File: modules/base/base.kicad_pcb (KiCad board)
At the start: 2 copper layers, 200.7 x 160 mm, 26 parts

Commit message: Add the version text
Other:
- board text added: "BASE 0.1.0"
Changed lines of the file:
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@@
+		)
+	)
+	(gr_text "BASE\n0.1.0"
+		(at 233.68 175.26 0)
+		(layer "F.SilkS")
+		(effects
+			(font
+				(size 2 2)
+				(thickness 0.4)
+				(bold yes)
+			)
+			(justify right bottom)
 		)
 	)

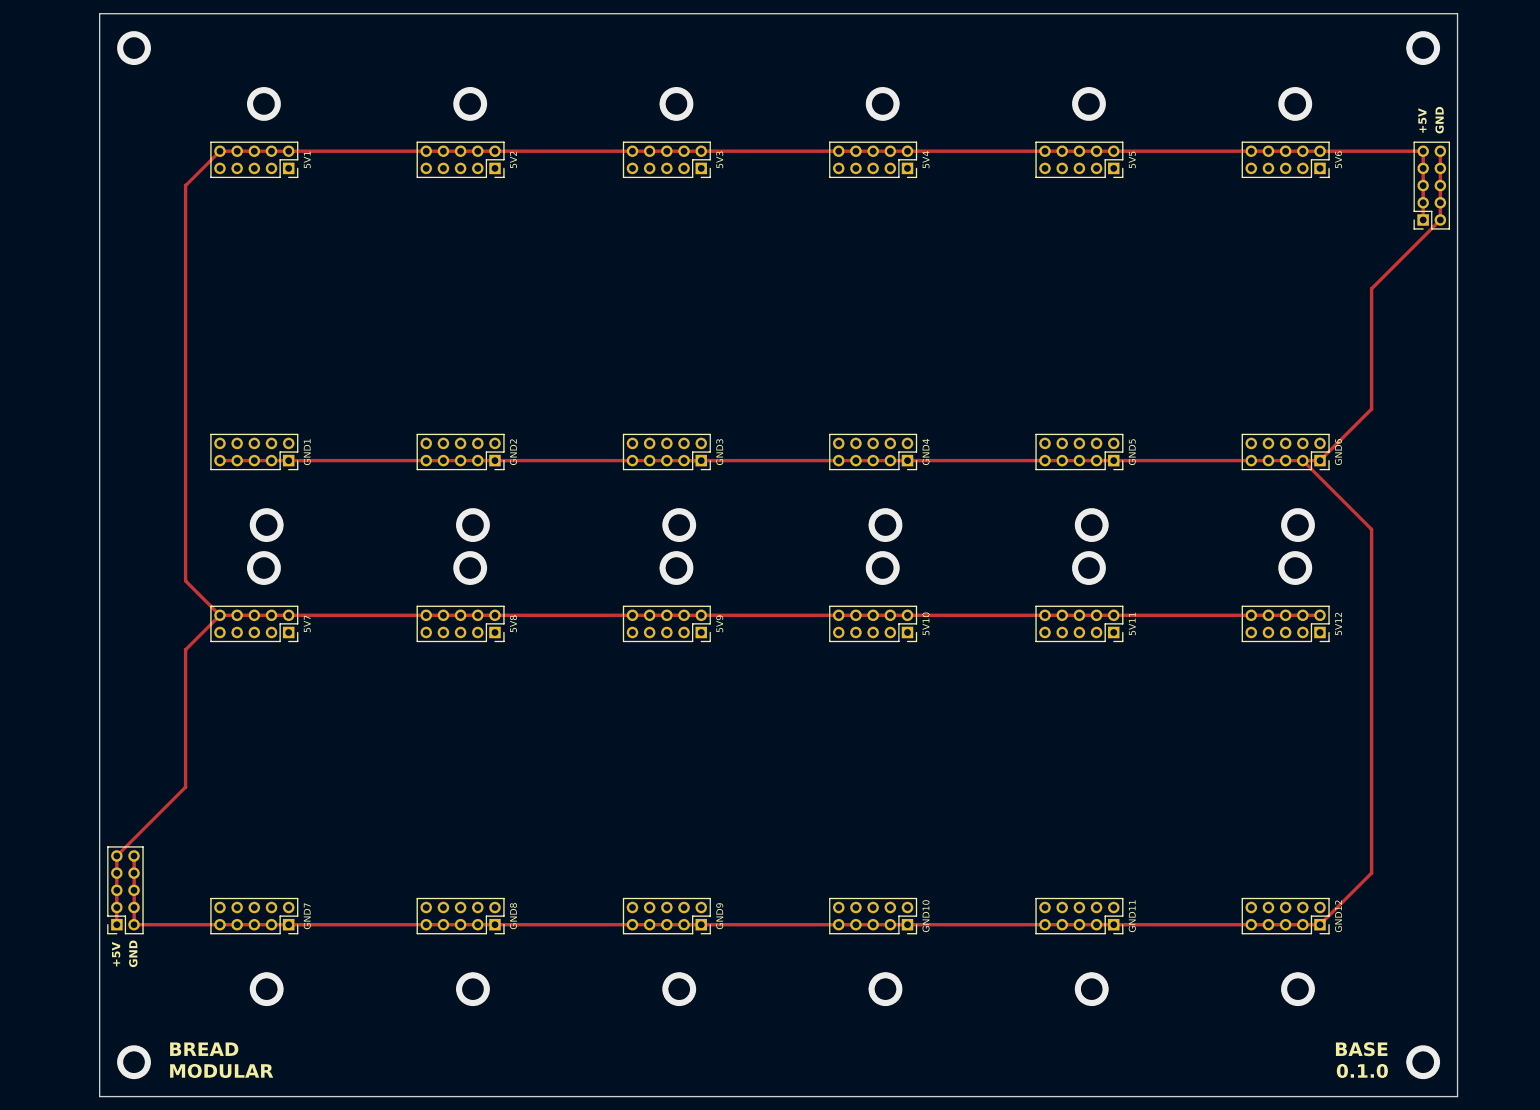
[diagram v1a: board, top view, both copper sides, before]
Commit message: Add power/gnd jacks
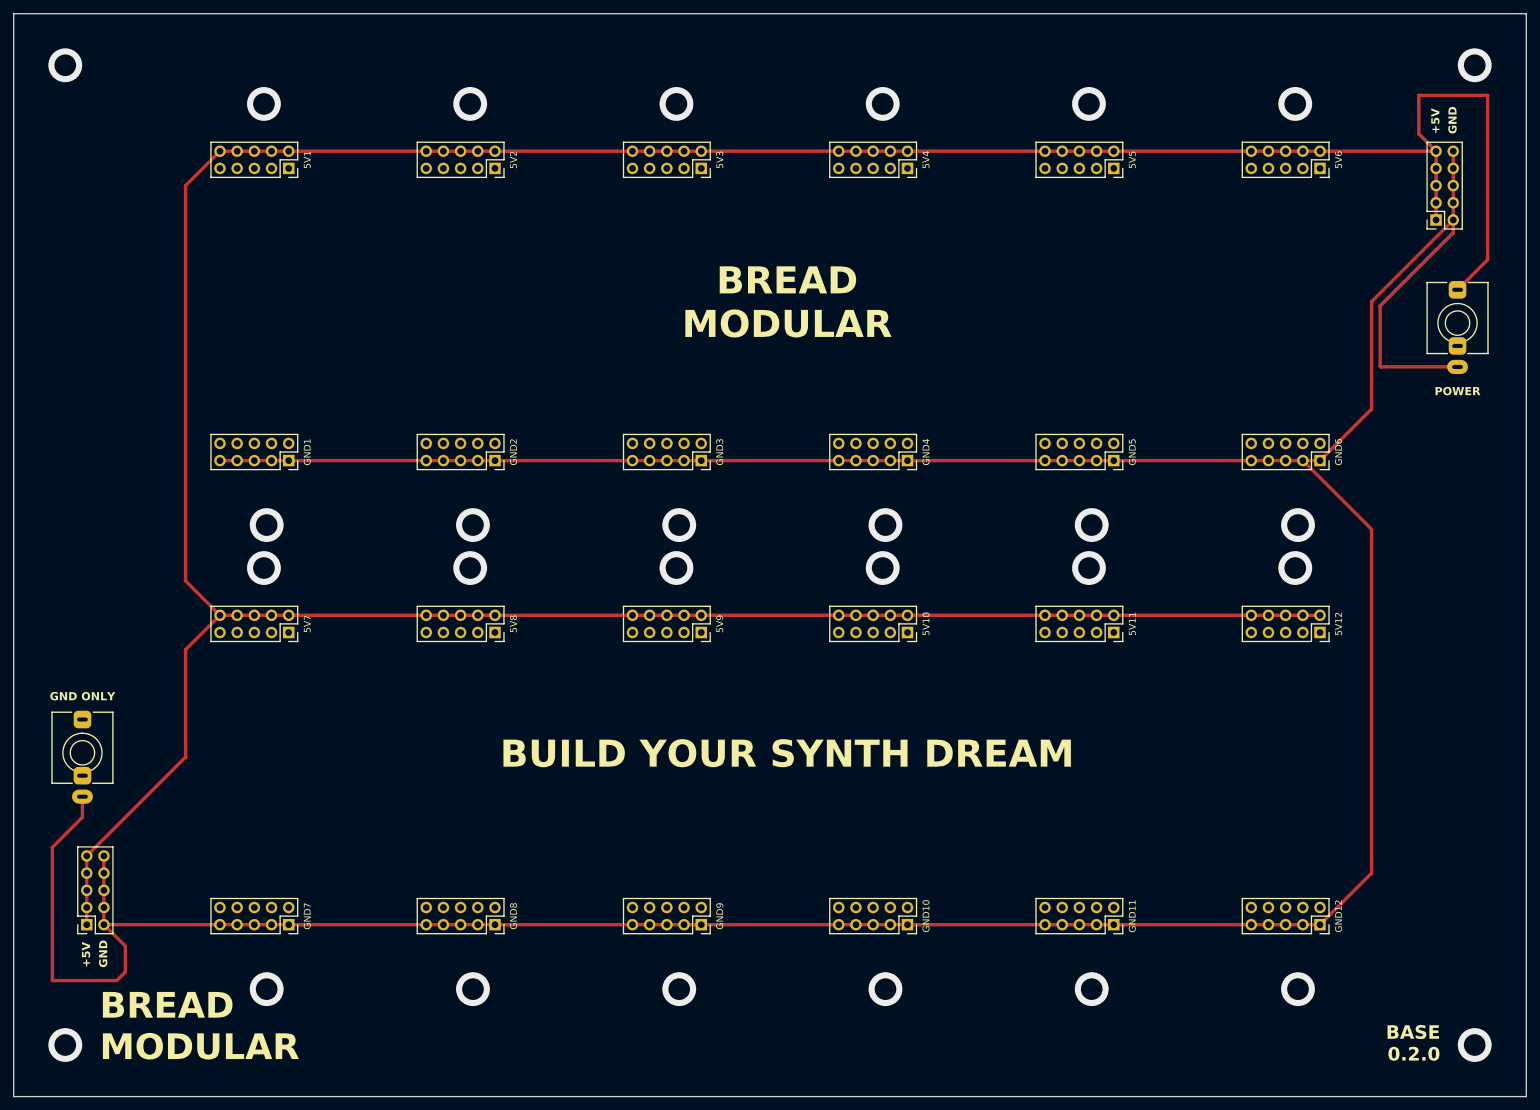
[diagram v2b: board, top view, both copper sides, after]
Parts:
- added J1: Power, BreadModular_AudioJacks:Jack_3.5mm_QingPu_WQP-PJ366ST_Vertical, F.Cu at (243.8, 63.5)
- added J2: Ground, BreadModular_AudioJacks:Jack_3.5mm_QingPu_WQP-PJ366ST_Vertical, F.Cu at (40.6, 127.0)
- moved 5V14 4.45 mm to (41.3, 152.4)
- moved 5V13 1.91 mm to (240.7, 48.3)
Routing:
- net GND: track 477.0 -> 568.4 mm
- net +5V: track 475.3 -> 529.1 mm
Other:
- board size 200.7 x 160 mm -> 223.5 x 160 mm
- board text added: "BASE 0.2.0"
- board text added: "BUILD YOUR SYNTH DREAM"
- board text added: "GND ONLY"
- board text added: "POWER"
- board text removed: "BASE 0.1.0"

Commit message: Add 2 jack sockets for cascading support.
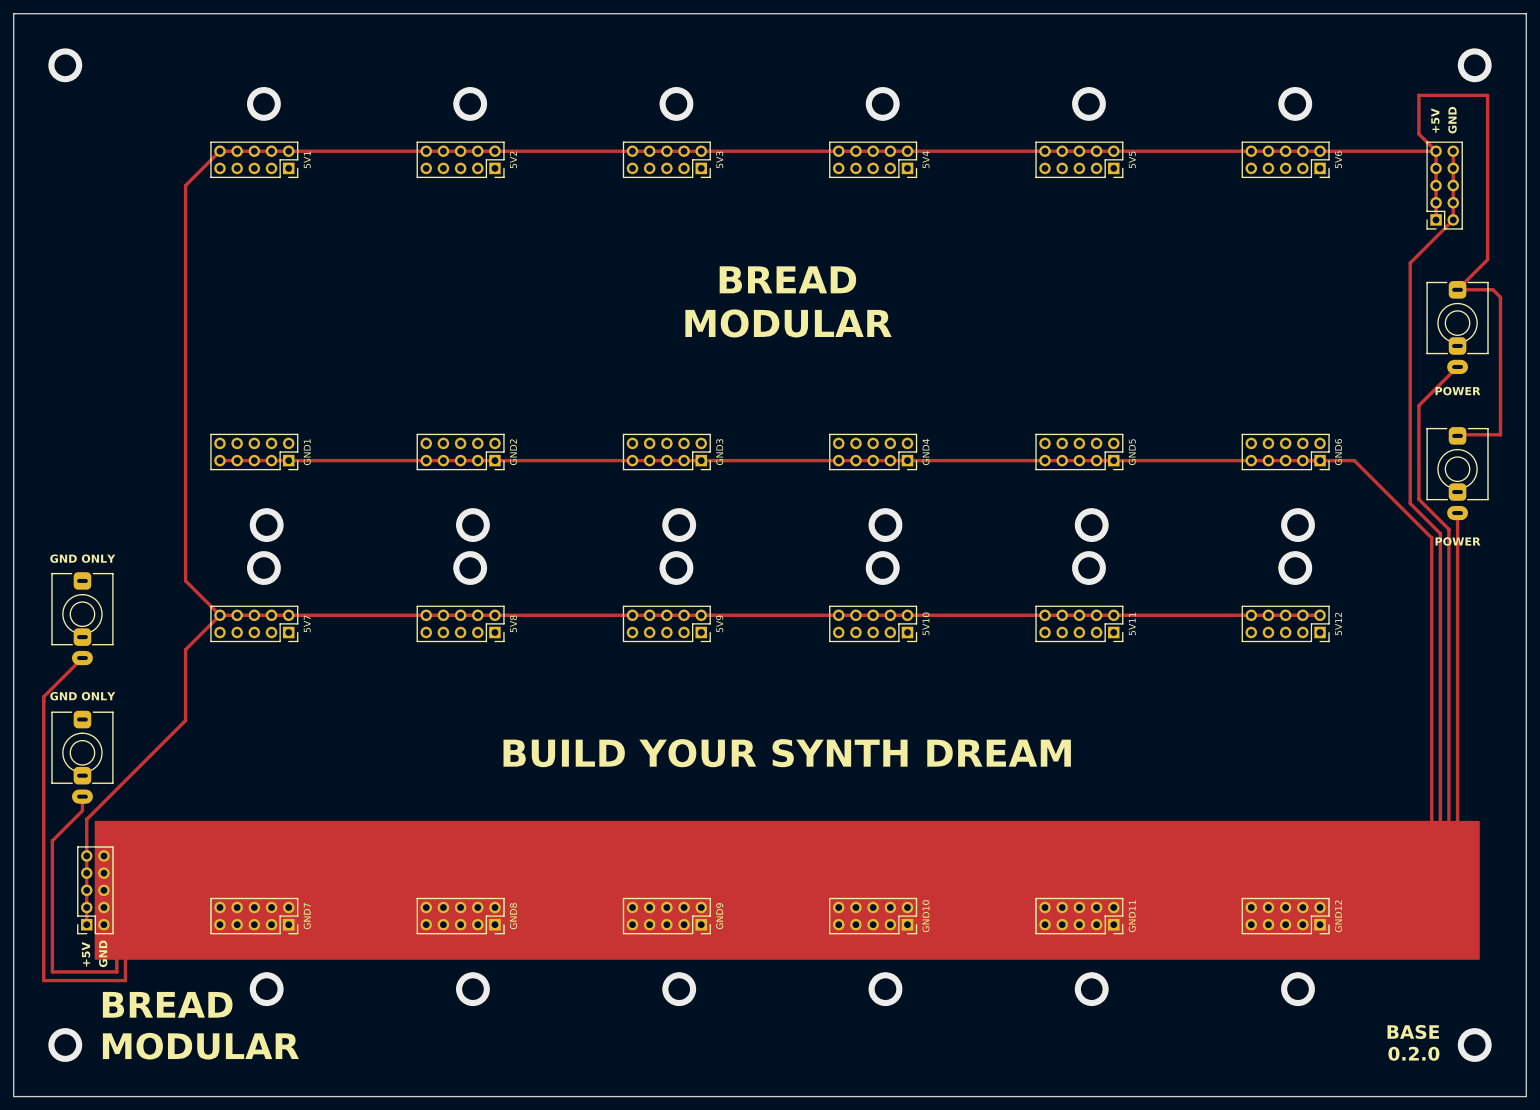
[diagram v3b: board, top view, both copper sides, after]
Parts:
- added J3: Power, BreadModular_AudioJacks:Jack_3.5mm_QingPu_WQP-PJ366ST_Vertical, F.Cu at (243.8, 85.1)
- added J4: Ground, BreadModular_AudioJacks:Jack_3.5mm_QingPu_WQP-PJ366ST_Vertical, F.Cu at (40.6, 106.5)
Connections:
- GND10 pad 10: unconnected-(GND10-Pin_10-Pad10) -> GND
- GND10 pad 2: unconnected-(GND10-Pin_2-Pad2) -> GND
- GND10 pad 4: unconnected-(GND10-Pin_4-Pad4) -> GND
- GND10 pad 6: unconnected-(GND10-Pin_6-Pad6) -> GND
- GND10 pad 8: unconnected-(GND10-Pin_8-Pad8) -> GND
- GND11 pad 10: unconnected-(GND11-Pin_10-Pad10) -> GND
- GND11 pad 2: unconnected-(GND11-Pin_2-Pad2) -> GND
- GND11 pad 4: unconnected-(GND11-Pin_4-Pad4) -> GND
- GND11 pad 6: unconnected-(GND11-Pin_6-Pad6) -> GND
- GND11 pad 8: unconnected-(GND11-Pin_8-Pad8) -> GND
- GND12 pad 10: unconnected-(GND12-Pin_10-Pad10) -> GND
- GND12 pad 2: unconnected-(GND12-Pin_2-Pad2) -> GND
- GND12 pad 4: unconnected-(GND12-Pin_4-Pad4) -> GND
- GND12 pad 6: unconnected-(GND12-Pin_6-Pad6) -> GND
- GND12 pad 8: unconnected-(GND12-Pin_8-Pad8) -> GND
- GND7 pad 10: unconnected-(GND7-Pin_10-Pad10) -> GND
- GND7 pad 2: unconnected-(GND7-Pin_2-Pad2) -> GND
- GND7 pad 4: unconnected-(GND7-Pin_4-Pad4) -> GND
- GND7 pad 6: unconnected-(GND7-Pin_6-Pad6) -> GND
- GND7 pad 8: unconnected-(GND7-Pin_8-Pad8) -> GND
- GND8 pad 10: unconnected-(GND8-Pin_10-Pad10) -> GND
- GND8 pad 2: unconnected-(GND8-Pin_2-Pad2) -> GND
- GND8 pad 4: unconnected-(GND8-Pin_4-Pad4) -> GND
- GND8 pad 6: unconnected-(GND8-Pin_6-Pad6) -> GND
- GND8 pad 8: unconnected-(GND8-Pin_8-Pad8) -> GND
- GND9 pad 10: unconnected-(GND9-Pin_10-Pad10) -> GND
- GND9 pad 2: unconnected-(GND9-Pin_2-Pad2) -> GND
- GND9 pad 4: unconnected-(GND9-Pin_4-Pad4) -> GND
- GND9 pad 6: unconnected-(GND9-Pin_6-Pad6) -> GND
- GND9 pad 8: unconnected-(GND9-Pin_8-Pad8) -> GND
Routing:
- net GND: track 568.4 -> 1320.9 mm
- net +5V: track 529.1 -> 561.3 mm

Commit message: base: Add USB power setup to the base
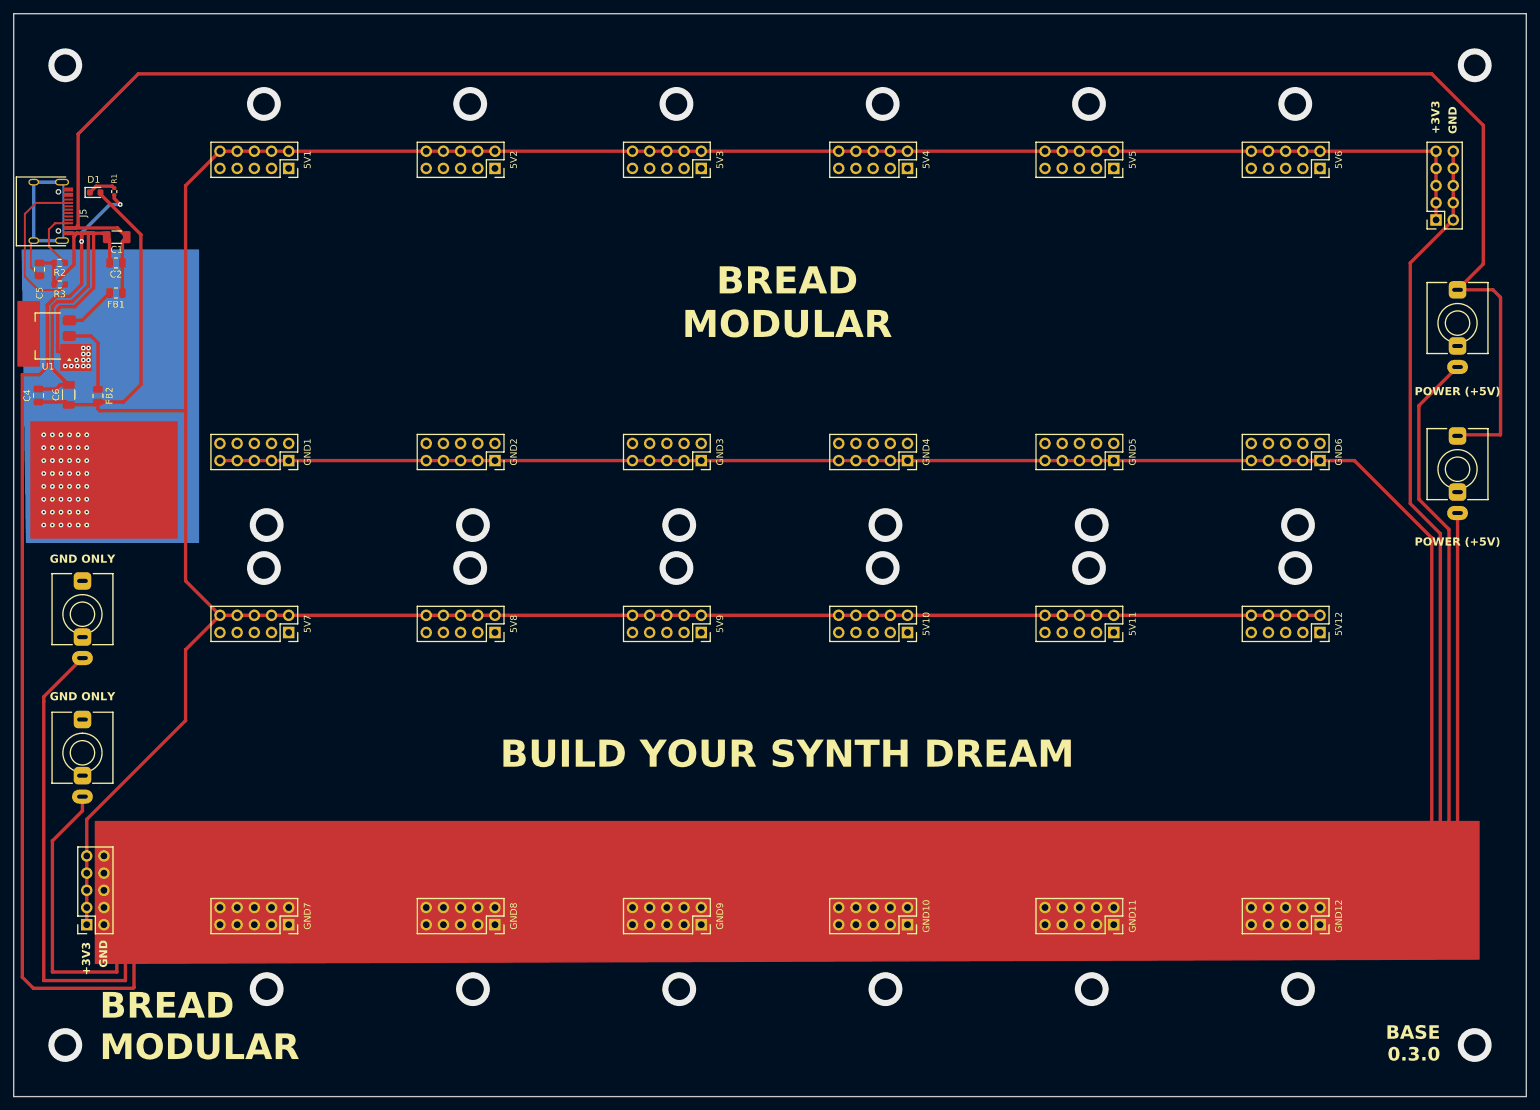
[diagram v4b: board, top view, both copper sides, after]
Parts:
- added C1: 100uf, Capacitor_SMD:C_1206_3216Metric, F.Cu at (45.7, 50.8)
- added C2: 0.1uf, Capacitor_SMD:C_0805_2012Metric, F.Cu at (45.6, 54.6)
- added C4: 0.1uf, Capacitor_SMD:C_0805_2012Metric, F.Cu at (34.1, 74.2)
- added C5: 10nf, Capacitor_SMD:C_0805_2012Metric, F.Cu at (34.3, 55.6)
- added C6: 100uf, Capacitor_SMD:C_1206_3216Metric, F.Cu at (38.6, 74.1)
- added D1: LED, LED_SMD:LED_0603_1608Metric, F.Cu at (42.5, 44.2)
- added FB1: GZ2012E800TF, Capacitor_SMD:C_0805_2012Metric, F.Cu at (45.6, 59.1)
- added FB2: GZ2012E800TF, Capacitor_SMD:C_0805_2012Metric, F.Cu at (42.9, 74.2)
- added J5: USB_C_Receptacle_PowerOnly_6P, BreadModular_TypeC:HRO-TYPE-C-31-M-12, F.Cu at (30.8, 47.0)
- added R1: 1k, Resistor_SMD:R_0402_1005Metric, F.Cu at (45.3, 44.1)
- added R2: 5.1k, Resistor_SMD:R_0603_1608Metric, F.Cu at (37.3, 54.6)
- added R3: 5.1k, Resistor_SMD:R_0603_1608Metric, F.Cu at (37.3, 57.8)
- added U1: AMS1117-3.3, Package_TO_SOT_SMD:SOT-223, F.Cu at (35.6, 65.4)
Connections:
- 5V1 pad 10: +5V -> +3.3V
- 5V1 pad 2: +5V -> +3.3V
- 5V1 pad 4: +5V -> +3.3V
- 5V1 pad 6: +5V -> +3.3V
- 5V1 pad 8: +5V -> +3.3V
- 5V10 pad 10: +5V -> +3.3V
- 5V10 pad 2: +5V -> +3.3V
- 5V10 pad 4: +5V -> +3.3V
- 5V10 pad 6: +5V -> +3.3V
- 5V10 pad 8: +5V -> +3.3V
- 5V11 pad 10: +5V -> +3.3V
- 5V11 pad 2: +5V -> +3.3V
- 5V11 pad 4: +5V -> +3.3V
- 5V11 pad 6: +5V -> +3.3V
- 5V11 pad 8: +5V -> +3.3V
- 5V12 pad 10: +5V -> +3.3V
- 5V12 pad 2: +5V -> +3.3V
- 5V12 pad 4: +5V -> +3.3V
- 5V12 pad 6: +5V -> +3.3V
- 5V12 pad 8: +5V -> +3.3V
- 5V13 pad 1: +5V -> +3.3V
- 5V13 pad 3: +5V -> +3.3V
- 5V13 pad 5: +5V -> +3.3V
- 5V13 pad 7: +5V -> +3.3V
- 5V13 pad 9: +5V -> +3.3V
- 5V14 pad 1: +5V -> +3.3V
- 5V14 pad 3: +5V -> +3.3V
- 5V14 pad 5: +5V -> +3.3V
- 5V14 pad 7: +5V -> +3.3V
- 5V14 pad 9: +5V -> +3.3V
- 5V2 pad 10: +5V -> +3.3V
- 5V2 pad 2: +5V -> +3.3V
- 5V2 pad 4: +5V -> +3.3V
- 5V2 pad 6: +5V -> +3.3V
- 5V2 pad 8: +5V -> +3.3V
- 5V3 pad 10: +5V -> +3.3V
- 5V3 pad 2: +5V -> +3.3V
- 5V3 pad 4: +5V -> +3.3V
- 5V3 pad 6: +5V -> +3.3V
- 5V3 pad 8: +5V -> +3.3V
- 5V4 pad 10: +5V -> +3.3V
- 5V4 pad 2: +5V -> +3.3V
- 5V4 pad 4: +5V -> +3.3V
- 5V4 pad 6: +5V -> +3.3V
- 5V4 pad 8: +5V -> +3.3V
- 5V5 pad 10: +5V -> +3.3V
- 5V5 pad 2: +5V -> +3.3V
- 5V5 pad 4: +5V -> +3.3V
- 5V5 pad 6: +5V -> +3.3V
- 5V5 pad 8: +5V -> +3.3V
- 5V6 pad 10: +5V -> +3.3V
- 5V6 pad 2: +5V -> +3.3V
- 5V6 pad 4: +5V -> +3.3V
- 5V6 pad 6: +5V -> +3.3V
- 5V6 pad 8: +5V -> +3.3V
- 5V7 pad 10: +5V -> +3.3V
- 5V7 pad 2: +5V -> +3.3V
- 5V7 pad 4: +5V -> +3.3V
- 5V7 pad 6: +5V -> +3.3V
- 5V7 pad 8: +5V -> +3.3V
- 5V8 pad 10: +5V -> +3.3V
- 5V8 pad 2: +5V -> +3.3V
- 5V8 pad 4: +5V -> +3.3V
- 5V8 pad 6: +5V -> +3.3V
- 5V8 pad 8: +5V -> +3.3V
- 5V9 pad 10: +5V -> +3.3V
- 5V9 pad 2: +5V -> +3.3V
- 5V9 pad 4: +5V -> +3.3V
- 5V9 pad 6: +5V -> +3.3V
- 5V9 pad 8: +5V -> +3.3V
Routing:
- net +3.3V: track 0.00 -> 540.6 mm
- net +5V: track 561.3 -> 305.4 mm
- net GND: track 1320.9 -> 1558.8 mm, vias 0 -> 62
- net Net-(J5-SHIELD): track 0.00 -> 31.7 mm
- net Net-(J5-CC1): track 0.00 -> 23.5 mm
- net Net-(U1-VO): track 0.00 -> 11.5 mm
- net Net-(J5-CC2): track 0.00 -> 9.18 mm
- net Net-(U1-VI): track 0.00 -> 7.61 mm
- net Net-(D1-K): track 0.00 -> 4.11 mm
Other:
- board text added: "+3V3"
- board text added: "BASE 0.3.0"
- board text added: "POWER (+5V)"
- board text removed: "+5V"
- board text removed: "BASE 0.2.0"
- board text removed: "POWER"
